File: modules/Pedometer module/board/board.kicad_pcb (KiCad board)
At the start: 2 copper layers, 45 x 30 mm, 22 parts, among them J1 BATTERY, J2 Conn_01x06, J3 Conn_01x06, J4 Conn_01x05, J5 Conn_01x04, J6 Conn_01x06, SW1 RESET, U1 ESP32-WROOM-32, U2 HT7533-1-SOT89, U3 LSM6DS3

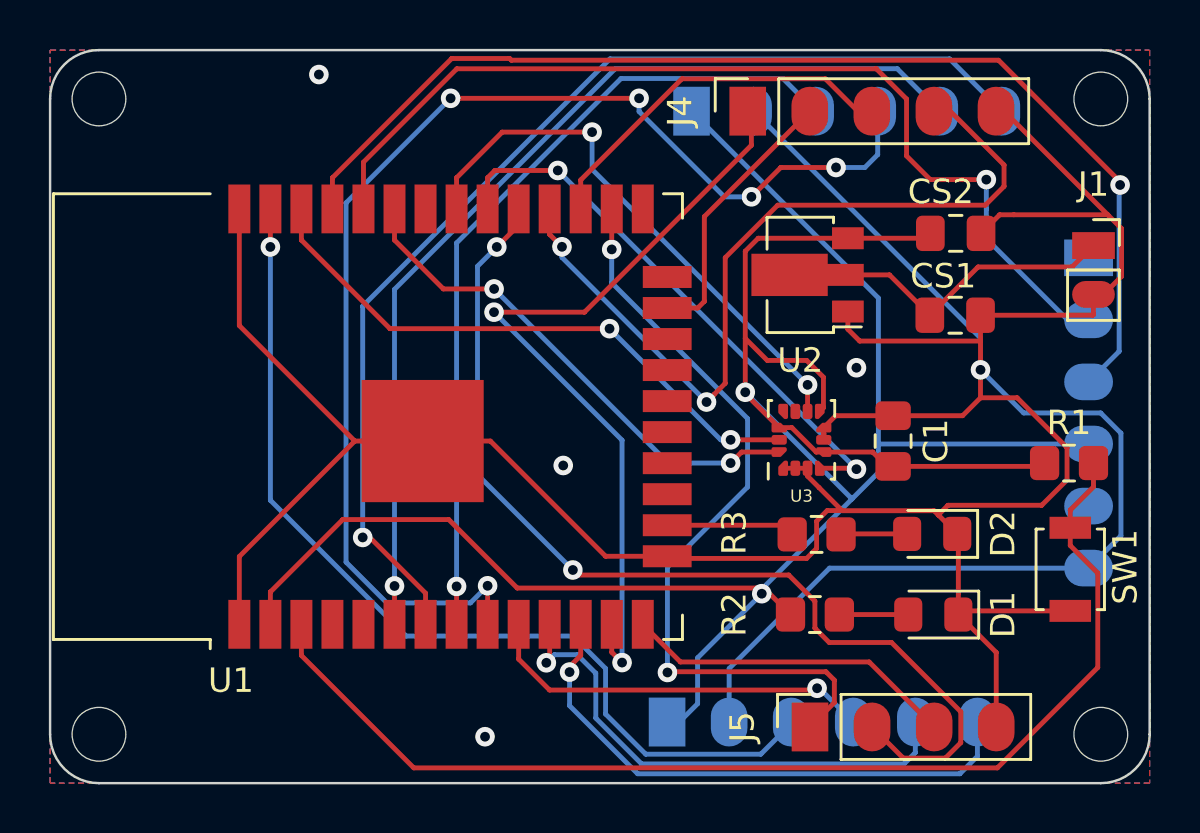
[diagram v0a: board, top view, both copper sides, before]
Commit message: Fix I2C pullup resistor
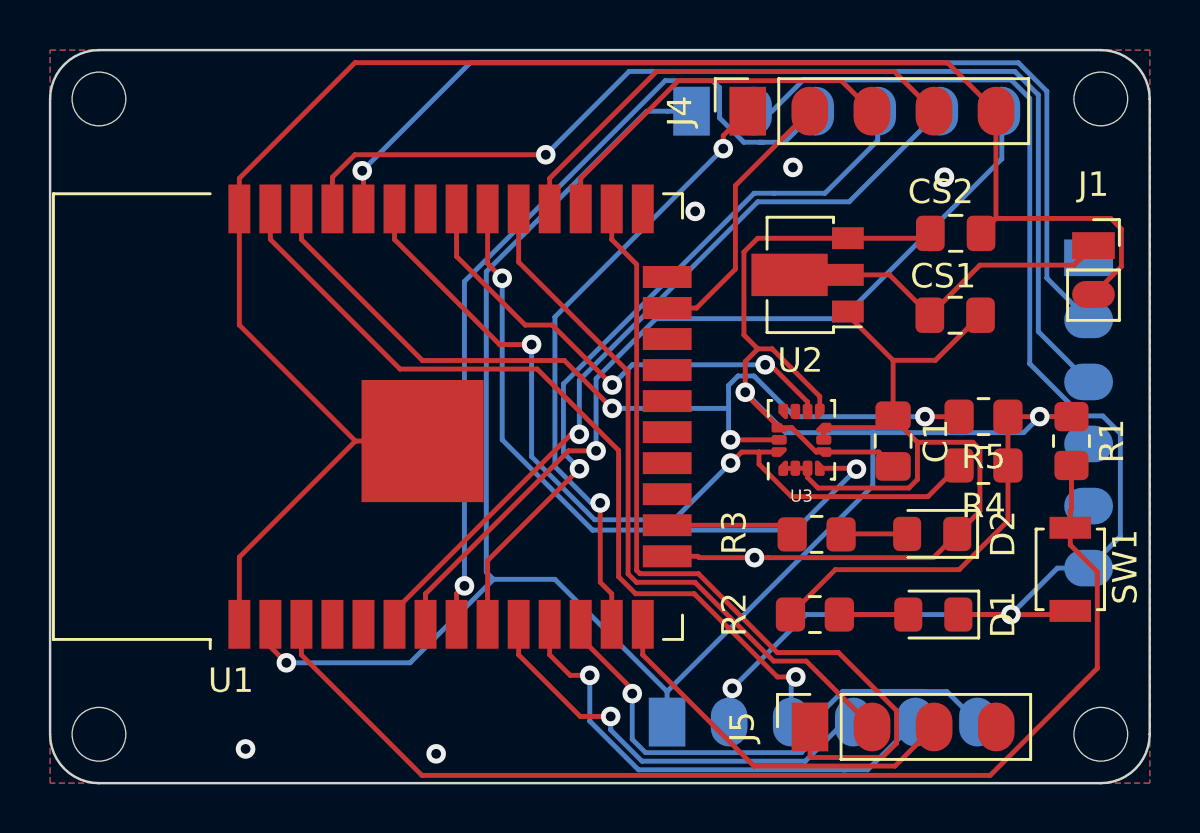
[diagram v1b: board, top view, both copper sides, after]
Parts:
- added R4: 10k, Resistor_SMD:R_0805_2012Metric_Pad1.20x1.40mm_HandSolder, F.Cu at (158.2, 97.0)
- added R5: 10k, Resistor_SMD:R_0805_2012Metric_Pad1.20x1.40mm_HandSolder, F.Cu at (158.2, 95.0)
- moved R1 0.91 mm to (161.8, 96.0), turned to 270 degrees
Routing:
- net /AUX_6: track 51.1 -> 29.9 mm, vias 5 -> 1
- net /1_4: track 34.6 -> 19.5 mm, vias 2 -> 0
- net SDA: track 21.0 -> 35.3 mm
- net +3V3: track 104.6 -> 118.2 mm, vias 2 -> 3
- net /2_2: track 41.7 -> 29.4 mm, vias 2 -> 0
- net SCL: track 24.2 -> 36.1 mm, vias 2 -> 3
- net /AUX_8: track 45.5 -> 35.9 mm
- net GND: track 162.3 -> 170.0 mm, vias 5 -> 8
- net /1_1: track 33.0 -> 25.4 mm
- net /AUX_7: track 40.5 -> 33.0 mm
- net INT1: track 23.1 -> 28.3 mm
- net /AUX_1: track 39.2 -> 35.1 mm
- net INT2: track 22.7 -> 19.8 mm
- net /2_1: track 31.9 -> 34.6 mm, vias 2 -> 0
- net /2_3: track 13.7 -> 15.7 mm
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
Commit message: PCB: USB C receptacle moved close to PCB edge
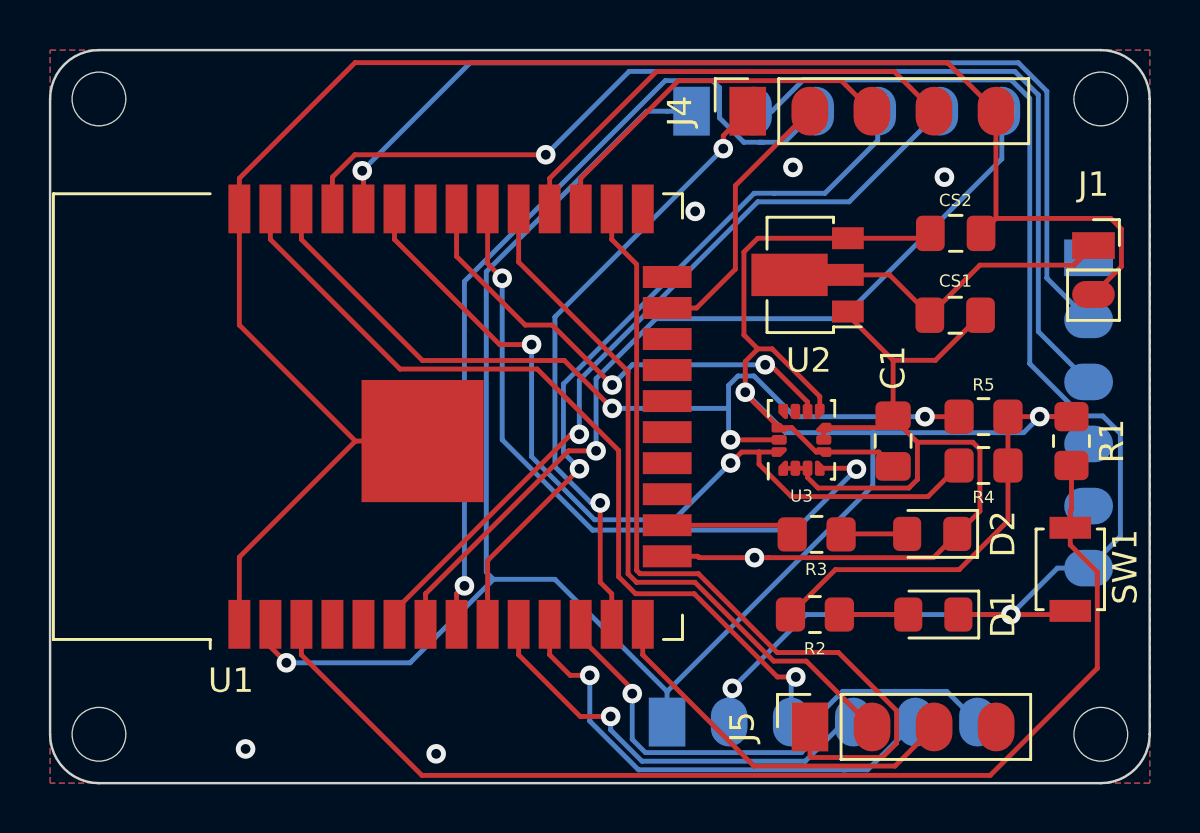
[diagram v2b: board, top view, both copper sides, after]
